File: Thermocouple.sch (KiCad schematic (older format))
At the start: 12 parts, among them U1 MCP3550-50-E/MS, U2 LM324, U3 MCP3550-50-E/MS

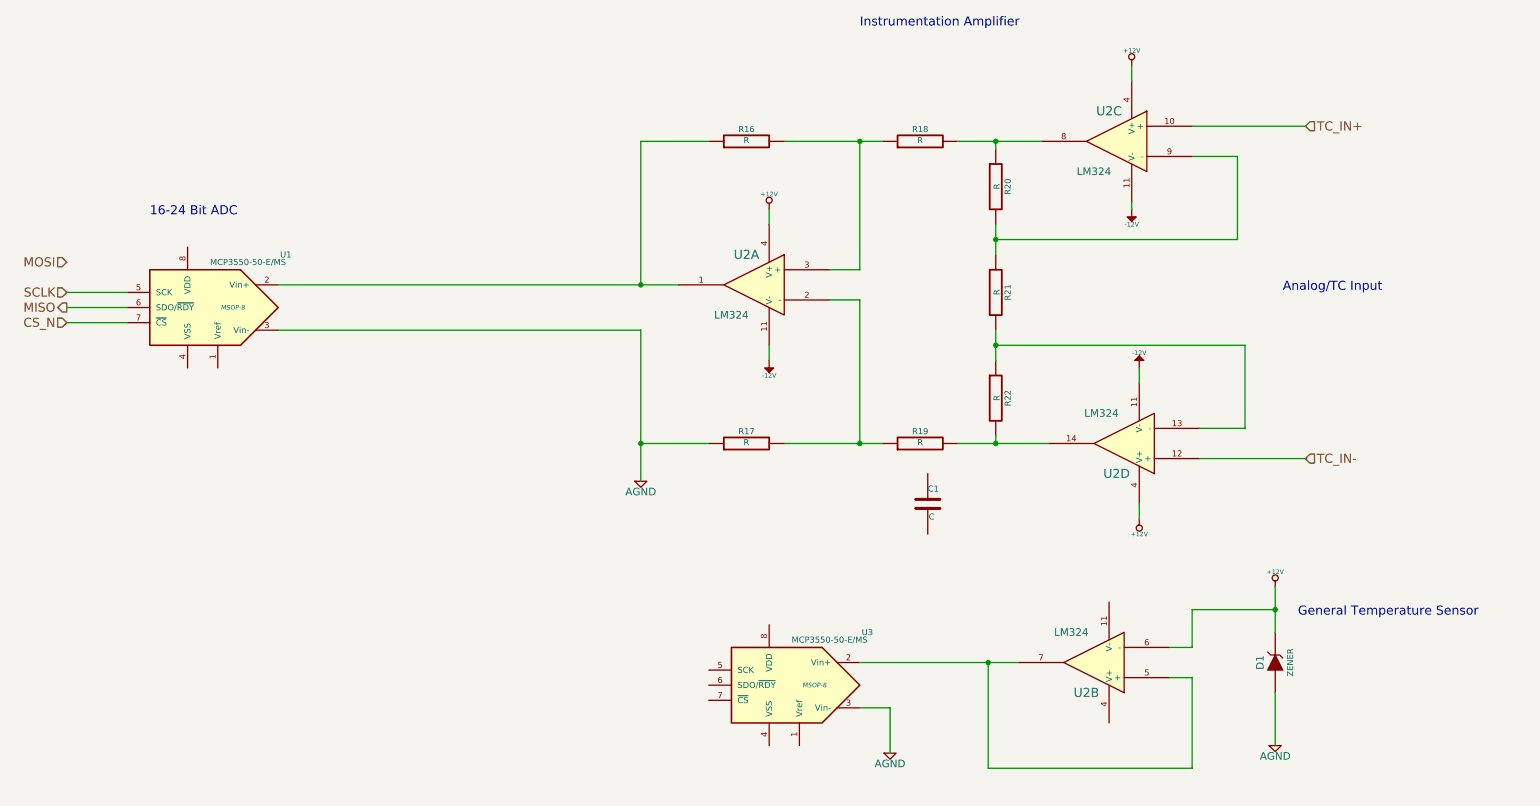
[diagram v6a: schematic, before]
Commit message: Associating and Placing the Thermocouple Module
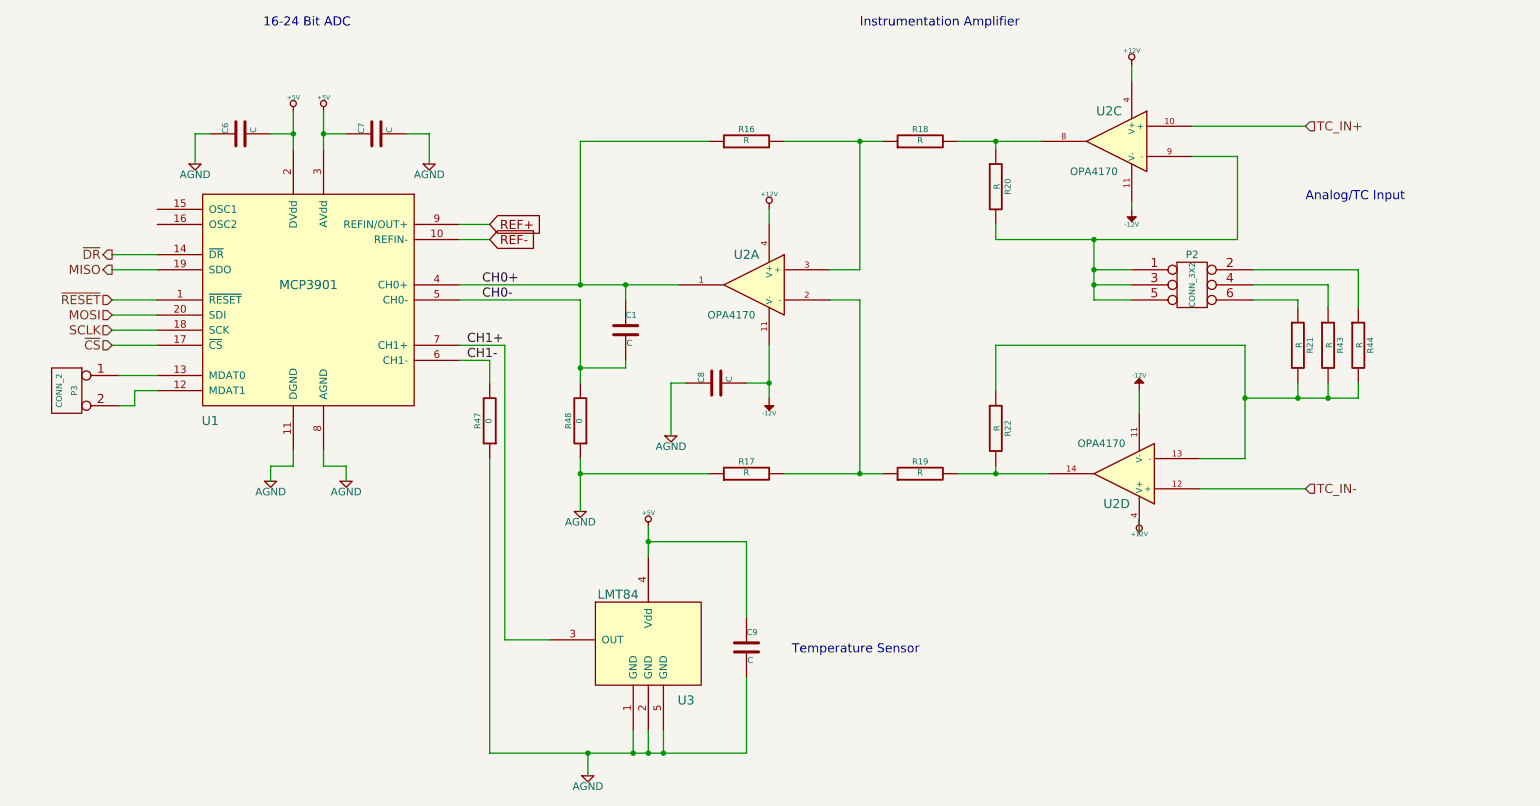
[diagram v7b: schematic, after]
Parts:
- removed D1: ZENER, symbol ZENER
- removed U1, U3: MCP3550-50-E/MS, MSOP-8, symbol MCP3550-50-E/MS
- removed unit 2 of U2
- added C6, C7, C8, C9: C, symbol C
- added P2: CONN_3X2, symbol CONN_3X2
- added P3: CONN_2, symbol CONN_2
- added R43, R44: R, symbol R
- added R47, R48: 0, symbol R
- added U1: MCP3901, symbol MCP3901
- added U3: LMT84, symbol LMT84
- U2: value LM324 -> OPA4170
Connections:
- net -12V: now also C8.2
- net AGND: now also C6.1, C7.2, C8.1, C9.2, R47.1, R48.1, U1.11 (DGND), U1.8 (AGND), U3.1 (GND), U3.2 (GND), U3.5 (GND)
- net MISO: now also U1.19 (SDO)
- net MOSI: now also U1.20 (SDI)
- net SCLK: now also U1.18 (SCK)
- net at R20.2, U2.9 (-): now also P2.1, P2.3, P2.5; no longer R21.1
- net at R21.2, R22.1, U2.13 (-): now also R43.2, R44.2
- net CH0+: now reaches C1.1
- net CH0+: now also R16.1, U2.1, U1.4 (CH0+)
- net CH0-: now reaches C1.2
- net CH0-: now also R48.2, U1.5 (CH0-)
- new net: P2.6, R21.1
- new net: P3.2 (PM), U1.12 (MDAT1)
- new net: P3.1 (P1), U1.13 (MDAT0)
- new net: P2.4, R43.1
- new net: P2.2, R44.1
- new net +5V: C6.2, C7.1, C9.1, U1.2 (DVdd), U1.3 (AVdd), U3.4 (Vdd)
- new net CH1+: U1.7 (CH1+), U3.3 (OUT)
- new net CH1-: R47.2, U1.6 (CH1-)
- new net REF+: U1.9 (REFIN/OUT+)
- new net REF-: U1.10 (REFIN-)
- new net ~CS: U1.17 (~CS)
- new net ~DR: U1.14 (~DR)
- new net ~RESET: U1.1 (~RESET)
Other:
- note added: "Temperature Sensor"
- note removed: "General Temperature Sensor"
- moved on the sheet: C1, R17, R19, R21, R22, U2D
